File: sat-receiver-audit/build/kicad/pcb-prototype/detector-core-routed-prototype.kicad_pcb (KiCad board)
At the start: 2 copper layers, 125 x 115 mm, 71 parts, among them Q450 AO3400A, Q451 AO3400A, Q452 AO3400A, Q453 AO3400A, Q454 AO3400A, Q455 AO3400A, Q456 AO3400A, Q457 AO3400A, U450 TLV3012BIDBVR, U451 TLV3012BIDBVR, U452 TLV3012BIDBVR, U453 TLV3012BIDBVR, U454 TLV3012BIDBVR, U455 TLV3012BIDBVR, U456 TLV3012BIDBVR, U457 TLV3012BIDBVR, U458 LM4040A20IDBZR 2.048 V 0.1% s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

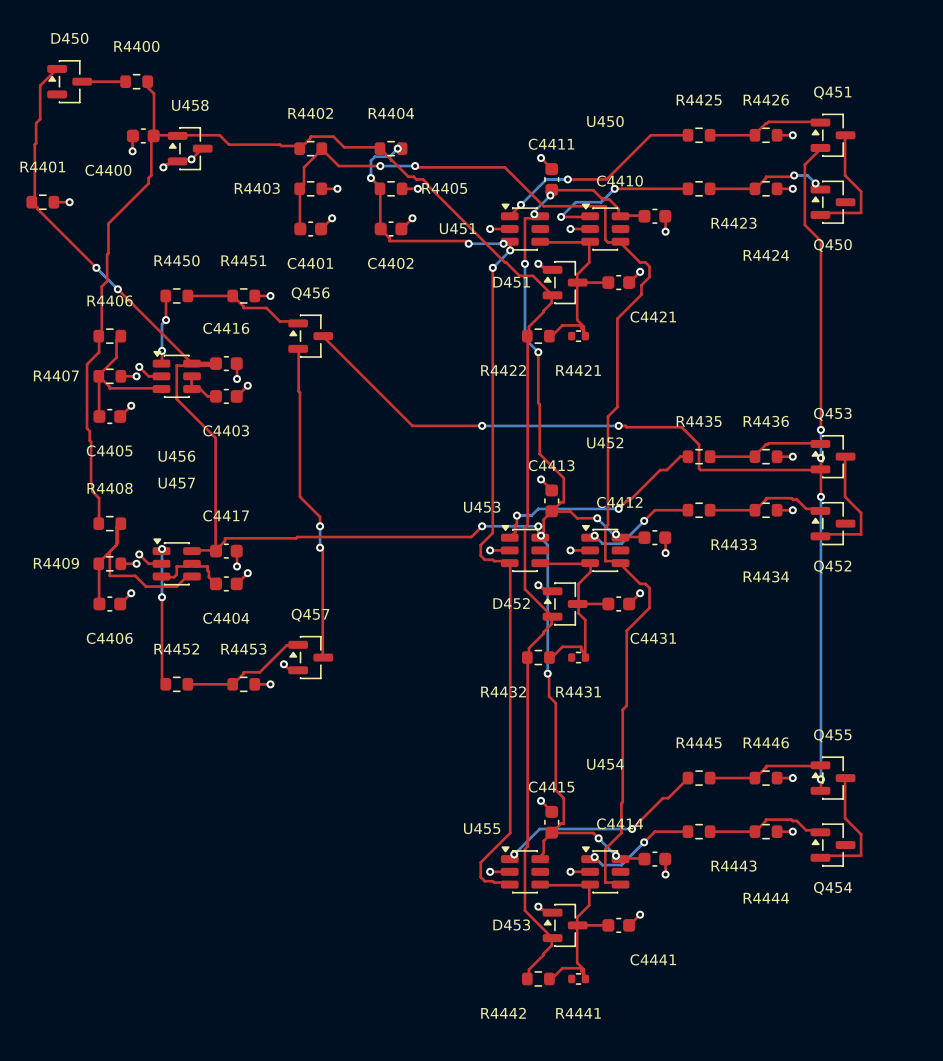
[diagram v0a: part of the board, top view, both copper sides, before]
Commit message: WIP: integration follow-ups
Made by the GPT/Codex run on 23.10.2026 (pushed as 5455b1e under the name "Claude");
re-attributed to Codex when integrated into ccr-1537979d-cj7q9t.
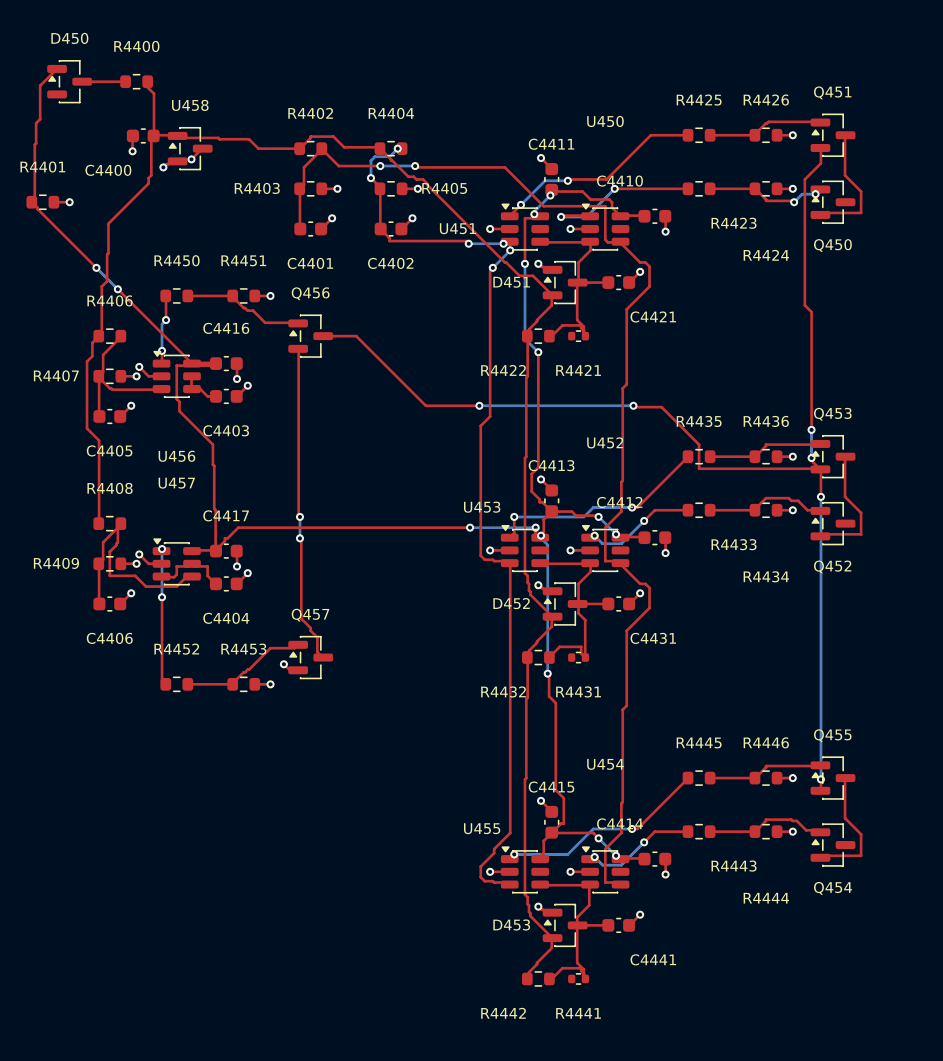
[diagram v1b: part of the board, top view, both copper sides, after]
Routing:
- net 3V3_Q6A: track 155.0 -> 154.4 mm
